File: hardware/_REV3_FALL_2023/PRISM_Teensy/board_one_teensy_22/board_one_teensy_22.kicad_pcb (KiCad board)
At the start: 2 copper layers, 61 x 88.9 mm, 31 parts, among them J1 DM3CS-SF, J2 CORE_IO, J3 3387, J3 USB_micro, U1 Teensy4.0, U3 3966, U5 LSM9DS1

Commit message: Procrastinated PRISM commit
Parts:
- moved LS1 58.4 mm to (114.3, 65.4)
- moved J1 48.6 mm to (133.4, 111.1), turned to 90 degrees
- moved J3 46.7 mm to (149.6, 72.0), turned to -90 degrees

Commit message: Finalized PRISM schematic
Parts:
- removed C4, C6: C_100nF, footprints:C_0603_1608Metric
- removed C5: C_10uF, footprints:C_0805_OEM
- removed C7: C_10nF, footprints:C_1206_OEM
- removed D1, D2: SS54, JLC_footprints:DO-214AC
- removed D4: 1655, neopixel:LED_1655
- removed J2: CORE_IO, Connector_JST:JST_PH_S7B-PH-K_1x07_P2.00mm_Horizontal
- removed LS1: SMT-0827-S-HT-R, buzzer:XDCR_SMT-0827-S-HT-R
- added J4: Conn_01x14, Connector_JST:JST_XH_B14B-XH-A_1x14_P2.50mm_Vertical, F.Cu at (193.9, 109.1)
- C3: value C_100nF -> 0.1uf; footprint footprints:C_0603_1608Metric -> Capacitor_SMD:C_0603_1608Metric
- D3: value 1655 -> WS2812B; footprint neopixel:LED_1655 -> LED_SMD:LED_WS2812B_PLCC4_5.0x5.0mm_P3.2mm
- J1: value DM3CS-SF -> Micro_SD_Card_Det_Hirose_DM3AT; footprint DM3:HRS_DM3CS-SF -> OEM:DM3CS-SF_HIR
- R1, R2, R3: value R_10K -> 10k; footprint footprints:R_0805_OEM -> Resistor_SMD:R_0603_1608Metric
- R4: value 200K -> 56k
- R5: value 300K -> 15k
- U3: footprint BMP388:Adafruit_Industries-3966-MFG -> Personal:MPL3115A2
- moved J1 72.1 mm to (204.2, 124.7)
- moved U1 61.6 mm to (189.9, 54.3), turned to 0 degrees
- moved J3 60.7 mm to (171.7, 105.7)
- moved U3 58.6 mm to (210.5, 97.4)
- moved R5 30.2 mm to (163.3, 44.1)
- moved J3 28.5 mm to (178.1, 73.5)
- moved C2 18.0 mm to (102.6, 105.2)
- moved R4 17.5 mm to (144.9, 46.1)
- moved C1 15.7 mm to (142.0, 46.1)
- moved D3 15.5 mm to (101.7, 114.1)
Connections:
- D3 pad 1: GND -> /5V
- D3 pad 2: /NEOPIXEL -> unconnected-(D3-DOUT-Pad2)
- D3 pad 3: /5V -> GND
- D3 pad 4: Net-(D3-Pad4) -> Net-(D3-DIN)
- D5 pad 1: unconnected-(D5-VDD-Pad1) -> /5V
- D5 pad 2: unconnected-(D5-DOUT-Pad2) -> Net-(D3-DIN)
- D5 pad 3: unconnected-(D5-VSS-Pad3) -> GND
- J1 pad 1: unconnected-(J1-DAT2-Pad1) -> Net-(J1-DAT2)
- J1 pad 2: unconnected-(J1-CD/DAT3-Pad2) -> /MISO
- J1 pad 3: unconnected-(J1-CMD-Pad3) -> /SD_CS
- J1 pad 5: unconnected-(J1-CLK-Pad5) -> /SD_SCK
- J1 pad 6: unconnected-(J1-VSS-Pad6) -> GND
- J1 pad 7: unconnected-(J1-DAT0-Pad7) -> /MOSI
- J1 pad 8: unconnected-(J1-DAT1-Pad8) -> Net-(J1-DAT1)
- J1 pad 9: unconnected-(J1-CD_SW-Pad9) -> /SD_Detect
- R1 pad 1: /3.3V -> Net-(J1-DET_A)
- R1 pad 2: /SCL 0 -> /3.3V
- R2 pad 1: /3.3V -> Net-(J1-DAT1)
- R2 pad 2: /SDA 0 -> Net-(J1-DET_A)
- R3 pad 2: Net-(U5-DEN_A/G) -> Net-(J1-DAT2)
- R4 pad 2: Net-(R4-Pad2) -> /V_Mon
- R5 pad 1: Net-(R4-Pad2) -> /V_Mon
- U1 pad 11: unconnected-(U1-9_OUT1C-Pad11) -> /SD_Detect
- U1 pad 12: unconnected-(U1-10_CS_MQSR-Pad12) -> /SD_CS
- U1 pad 13: unconnected-(U1-11_MOSI_CTX1-Pad13) -> /MOSI
- U1 pad 14: unconnected-(U1-12_MISO_MQSL-Pad14) -> /MISO
- U1 pad 2: unconnected-(U1-0_RX1_CRX2_CS1-Pad2) -> /RX_GPS
- U1 pad 20: unconnected-(U1-13_SCK_CRX1_LED-Pad20) -> /SD_SCK
- U1 pad 3: unconnected-(U1-1_TX1_CTX2_MISO1-Pad3) -> /TX_GPS
- U1 pad 30: unconnected-(U1-23_A9_CRX1_MCLK1-Pad30) -> /V_Mon
- U1 pad 7: unconnected-(U1-5_IN2-Pad7) -> /Radio_RST
- U1 pad 8: unconnected-(U1-6_OUT1D-Pad8) -> /CS 1
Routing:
- net GND: track 3.42 -> 0.00 mm
- net /PYRO 2: track 0.77 -> 0.00 mm
- net /CONT 1: track 0.63 -> 0.00 mm
- net /5V: track 0.59 -> 0.00 mm

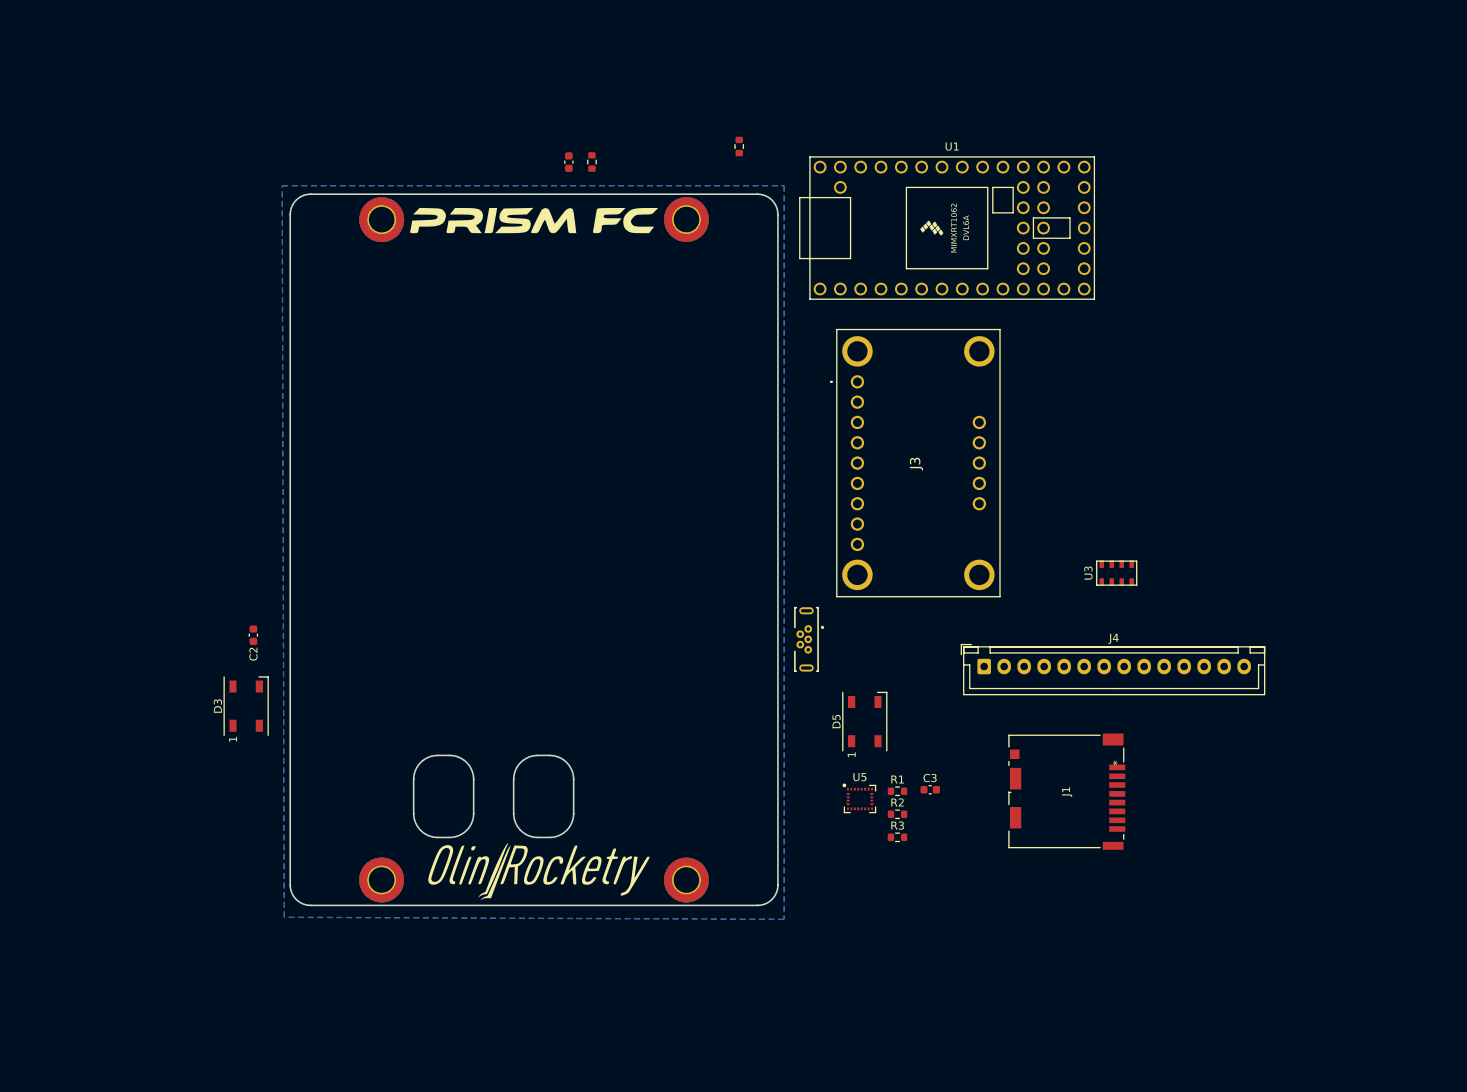
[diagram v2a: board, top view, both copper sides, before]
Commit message: Fix file name issue
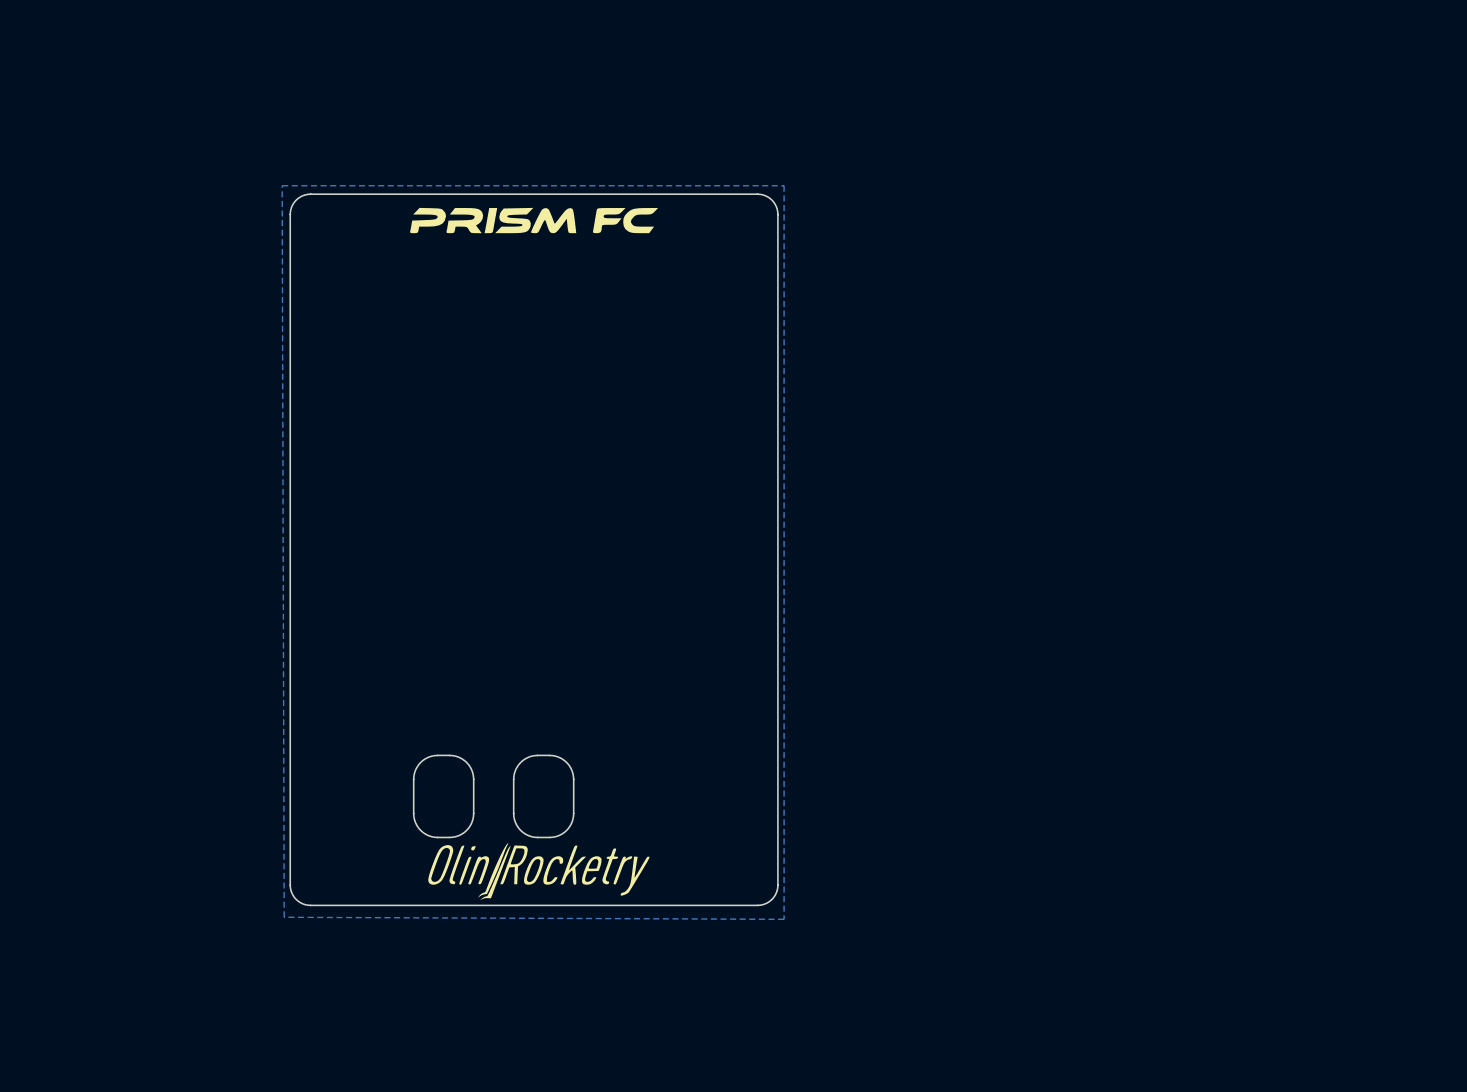
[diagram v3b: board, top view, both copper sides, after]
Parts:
- removed C1, C2, C3: 0.1uf, Capacitor_SMD:C_0603_1608Metric
- removed D3, D5: WS2812B, LED_SMD:LED_WS2812B_PLCC4_5.0x5.0mm_P3.2mm
- removed H1: MountingHole_Pad, MountingHole:MountingHole_3.2mm_M3_DIN965_Pad_TopBottom
- removed H2, H3, H4: MountingHole, MountingHole:MountingHole_3.2mm_M3_DIN965_Pad_TopBottom
- removed J1: Micro_SD_Card_Det_Hirose_DM3AT, OEM:DM3CS-SF_HIR
- removed J3: 3387, LSM9DS1:3387
- removed J3: USB_micro, USB:GCT_USB3131-30-0230-A_REVB
- removed J4: Conn_01x14, Connector_JST:JST_XH_B14B-XH-A_1x14_P2.50mm_Vertical
- removed R1, R2, R3: 10k, Resistor_SMD:R_0603_1608Metric
- removed R4: 56k, Resistor_SMD:R_0603_1608Metric
- removed R5: 15k, Resistor_SMD:R_0603_1608Metric
- removed U1: Teensy4.0, Teensy_4.1:Teensy40
- removed U3: 3966, Personal:MPL3115A2
- removed U5: LSM9DS1, Package_LGA:LGA-24L_3x3.5mm_P0.43mm

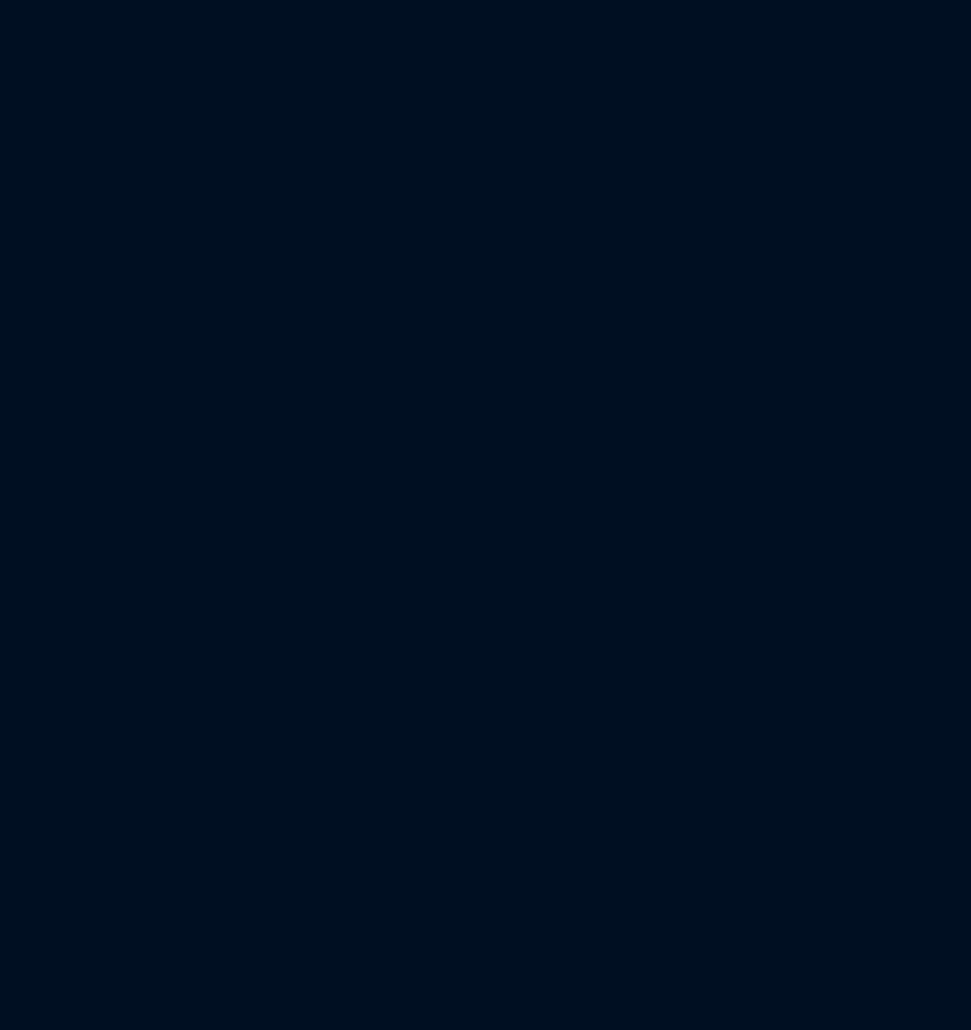
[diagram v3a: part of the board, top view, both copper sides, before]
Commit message: Need to fix SD slot still
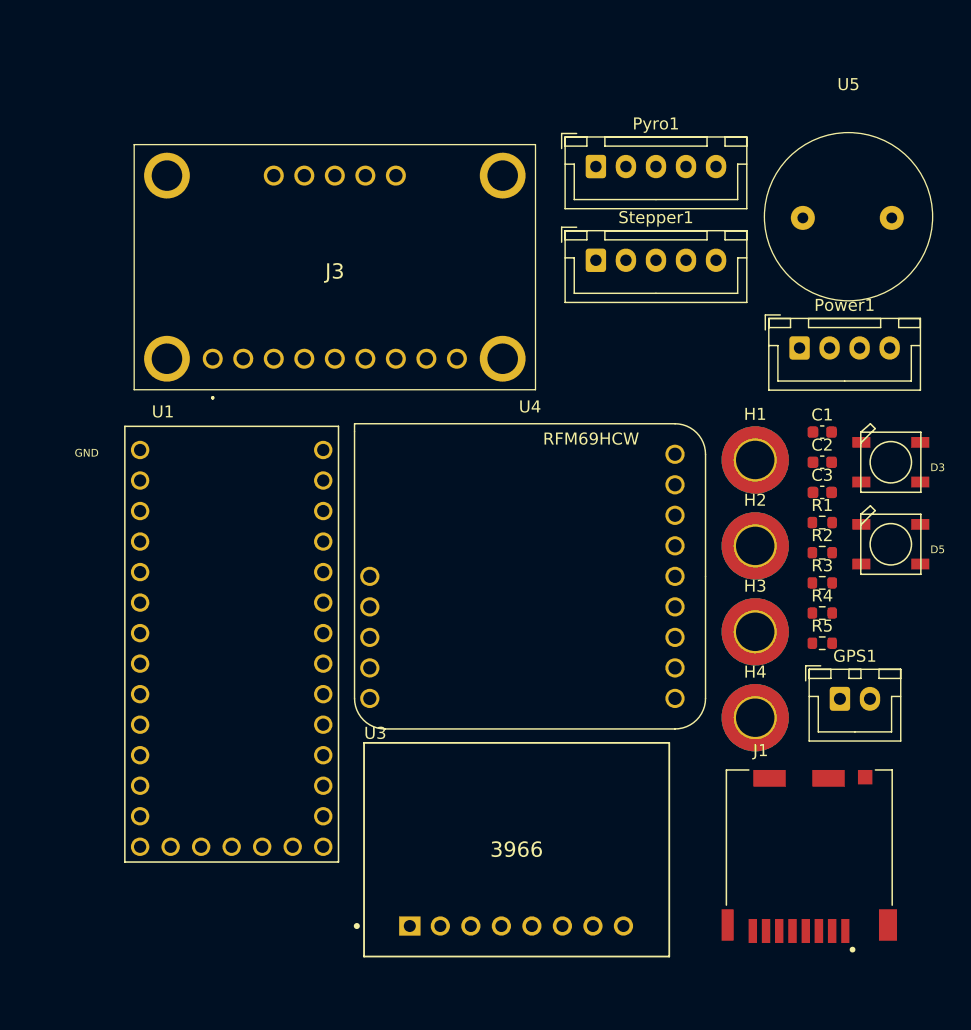
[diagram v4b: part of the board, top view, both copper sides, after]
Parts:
- added C1: 0.1uf, Capacitor_SMD:C_0603_1608Metric, F.Cu at (238.3, 93.0)
- added C2: 0.1uf, Capacitor_SMD:C_0603_1608Metric, F.Cu at (238.3, 95.5)
- added C3: 0.1uf, Capacitor_SMD:C_0603_1608Metric, F.Cu at (238.3, 98.0)
- added D3: WS2812B, rocketry_footprints:WS2812B, F.Cu at (244.0, 95.5)
- added D5: WS2812B, rocketry_footprints:WS2812B, F.Cu at (244.0, 102.3)
- added GPS1: Conn_01x02_Socket, Connector_JST:JST_XH_B2B-XH-A_1x02_P2.50mm_Vertical, F.Cu at (239.8, 115.2)
- added H1: MountingHole, MountingHole:MountingHole_3.2mm_M3_DIN965_Pad_TopBottom, F.Cu at (232.8, 95.3)
- added H2: MountingHole, MountingHole:MountingHole_3.2mm_M3_DIN965_Pad_TopBottom, F.Cu at (232.8, 102.5)
- added H3: MountingHole, MountingHole:MountingHole_3.2mm_M3_DIN965_Pad_TopBottom, F.Cu at (232.8, 109.6)
- added H4: MountingHole, MountingHole:MountingHole_3.2mm_M3_DIN965_Pad_TopBottom, F.Cu at (232.8, 116.8)
- added J1: Micro_SD_Card_Det_Hirose_DM3AT, rocketry_footprints:HRS_DM3CS-SF, F.Cu at (237.1, 128.2)
- added J3: 3387, rocketry_footprints:3387, F.Cu at (187.6, 86.9)
- added Power1: Conn_01x04_Socket, Connector_JST:JST_XH_B4B-XH-A_1x04_P2.50mm_Vertical, F.Cu at (236.4, 86.0)
- added Pyro1: Conn_01x05_Socket, Connector_JST:JST_XH_B5B-XH-A_1x05_P2.50mm_Vertical, F.Cu at (219.5, 70.9)
- added R1: 10k, Resistor_SMD:R_0603_1608Metric, F.Cu at (238.3, 100.5)
- added R2: 10k, Resistor_SMD:R_0603_1608Metric, F.Cu at (238.3, 103.0)
- added R3: 10k, Resistor_SMD:R_0603_1608Metric, F.Cu at (238.3, 105.5)
- added R4: 56k, Resistor_SMD:R_0603_1608Metric, F.Cu at (238.3, 108.0)
- added R5: 15k, Resistor_SMD:R_0603_1608Metric, F.Cu at (238.3, 110.5)
- added Stepper1: Conn_01x05_Socket, Connector_JST:JST_XH_B5B-XH-A_1x05_P2.50mm_Vertical, F.Cu at (219.5, 78.7)
- added U1: Teensy4.0, rocketry_footprints:MODULE_DEV-15583, F.Cu at (189.2, 111.0)
- added U3: 3966, rocketry_footprints:Adafruit_Industries-3966-MFG, F.Cu at (212.9, 127.7)
- added U4: RFM69HCW_Breakout, rocketry_footprints:RFM69HCW_Breakout, F.Cu at (214.0, 105.0)
- added U5: SFN-1407PA7.6, rocketry_footprints:SFN-1407PA7.6, F.Cu at (240.5, 75.2)

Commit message: PRISM FC built without errors
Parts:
- moved GPS1 5.81 mm to (240.2, 109.4)
- moved J1 5.81 mm to (237.4, 122.3)
- moved R1 5.81 mm to (238.7, 94.7)
- moved R4 5.81 mm to (238.7, 102.2)
- moved Stepper1 5.81 mm to (219.9, 72.9)
- moved D3 5.81 mm to (244.4, 89.7)
- moved D5 5.81 mm to (244.4, 96.5)
- moved H1 5.81 mm to (233.2, 89.5)
- moved H2 5.81 mm to (233.2, 96.7)
- moved H3 5.81 mm to (233.2, 103.8)
- moved H4 5.81 mm to (233.2, 111.0)
- moved J3 5.81 mm to (188.0, 81.1)
- moved Power1 5.81 mm to (236.8, 80.2)
- moved U1 5.81 mm to (189.6, 105.2)
- moved U4 5.81 mm to (214.4, 99.2)
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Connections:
- J1 pad 9: /SD_Detect -> Net-(J1-DET_A)
- R1 pad 2: /3.3V -> GND
- R2 pad 2: Net-(J1-DET_A) -> /3.3V
- U1 pad 14: /SD_Detect -> GND

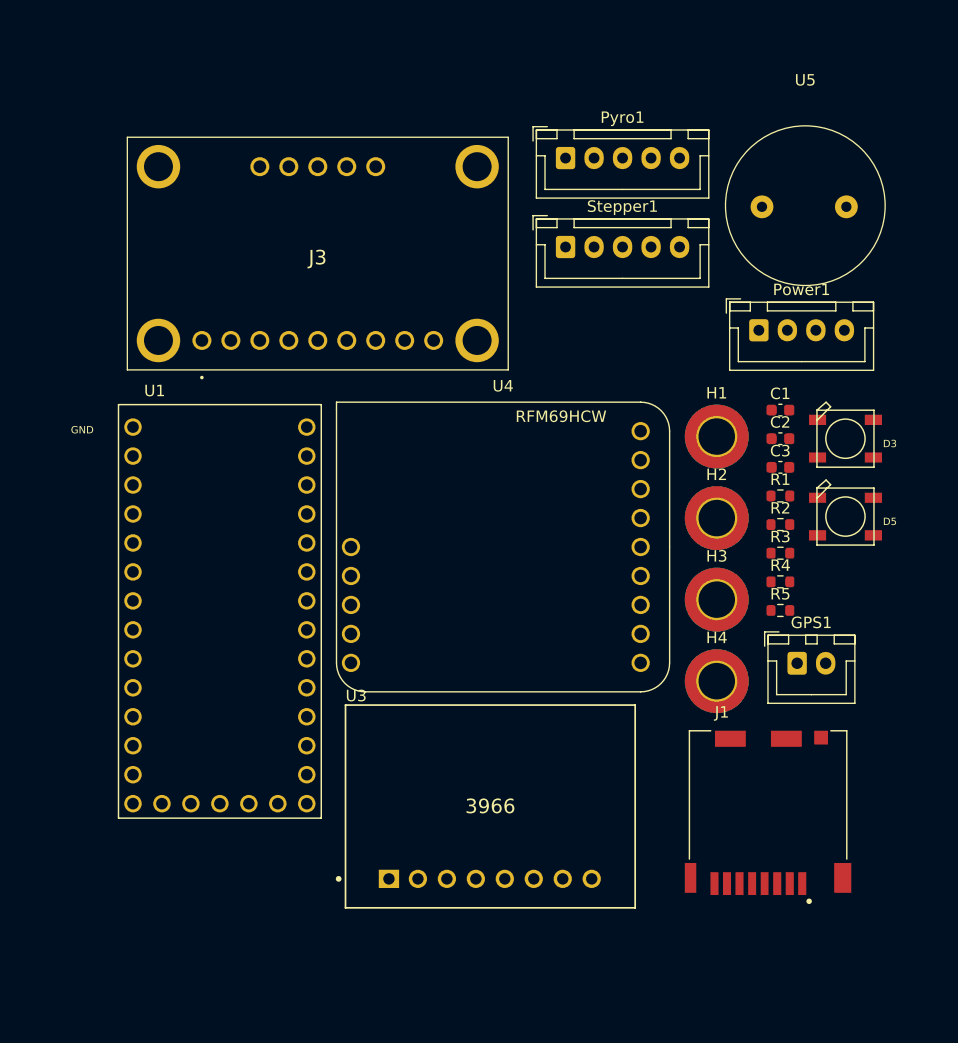
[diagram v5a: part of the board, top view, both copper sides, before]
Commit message: Fix SD Detect error
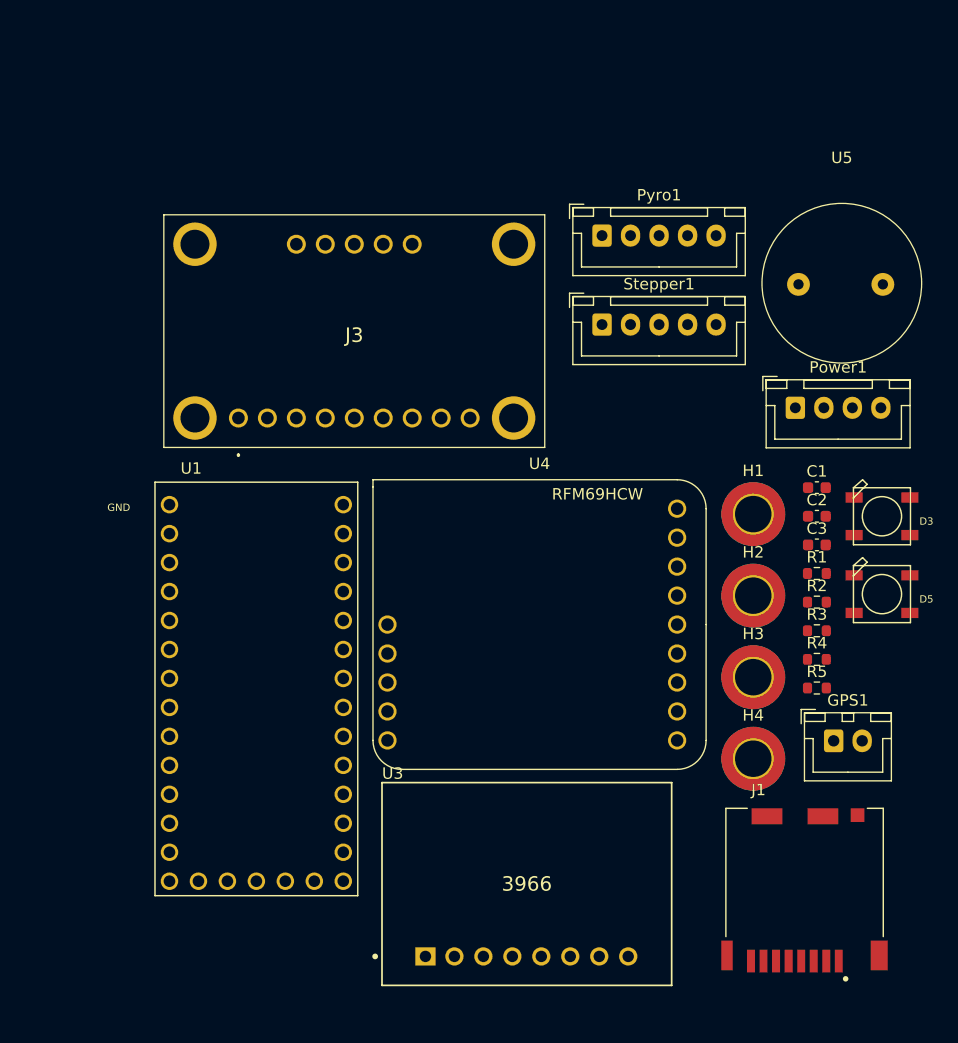
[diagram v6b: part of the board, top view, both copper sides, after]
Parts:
- moved GPS1 7.52 mm to (243.4, 116.2)
- moved J1 7.52 mm to (240.7, 129.2)
- moved R1 7.52 mm to (241.9, 101.5)
- moved R4 7.52 mm to (241.9, 109.0)
- moved Stepper1 7.52 mm to (223.1, 79.7)
- moved U3 7.52 mm to (216.5, 128.7)
- moved C1 7.52 mm to (241.9, 94.0)
- moved C2 7.52 mm to (241.9, 96.5)
- moved C3 7.52 mm to (241.9, 99.0)
- moved J3 7.52 mm to (191.2, 87.9)
- moved Pyro1 7.52 mm to (223.1, 71.9)
- moved R2 7.52 mm to (241.9, 104.0)
- moved R3 7.52 mm to (241.9, 106.5)
- moved R5 7.52 mm to (241.9, 111.5)
- moved U4 7.52 mm to (217.6, 106.0)
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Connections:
- J1 pad 9: Net-(J1-DET_A) -> /SD_DETECT
- R1 pad 1: Net-(J1-DET_A) -> /SD_DETECT
- R1 pad 2: GND -> /3.3V
- U1 pad 14: GND -> /SD_DETECT
